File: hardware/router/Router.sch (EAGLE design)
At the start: 52 parts, among them J1 AVR_PROG, J10 RJ45-8PTH, J11 RJ45-8PTH, J12 RJ45-8PTH, J13 RJ45-8PTH, J14 RJ45-8PTH, J15 RJ45-8PTH, J16 RJ45-8PTH, J17 RASPBERRYPI_BB, J18 RJ45-8PTH, J19 RJ45-8PTH, J2 RJ45-8PTH, J3 RJ45-8PTH, J4 RJ45-8PTH, J5 RJ45-8PTH, J6 RJ45-8PTH, J7 RJ45-8PTH, J8 RJ45-8PTH, J9 RJ45-8PTH, Q1 NMOS, Q2 NMOS, Q3 NMOS, U1 ATMEGA168, U3 DS1307SO8, U6 CON-MATENLOK, Y1 32.768kHz

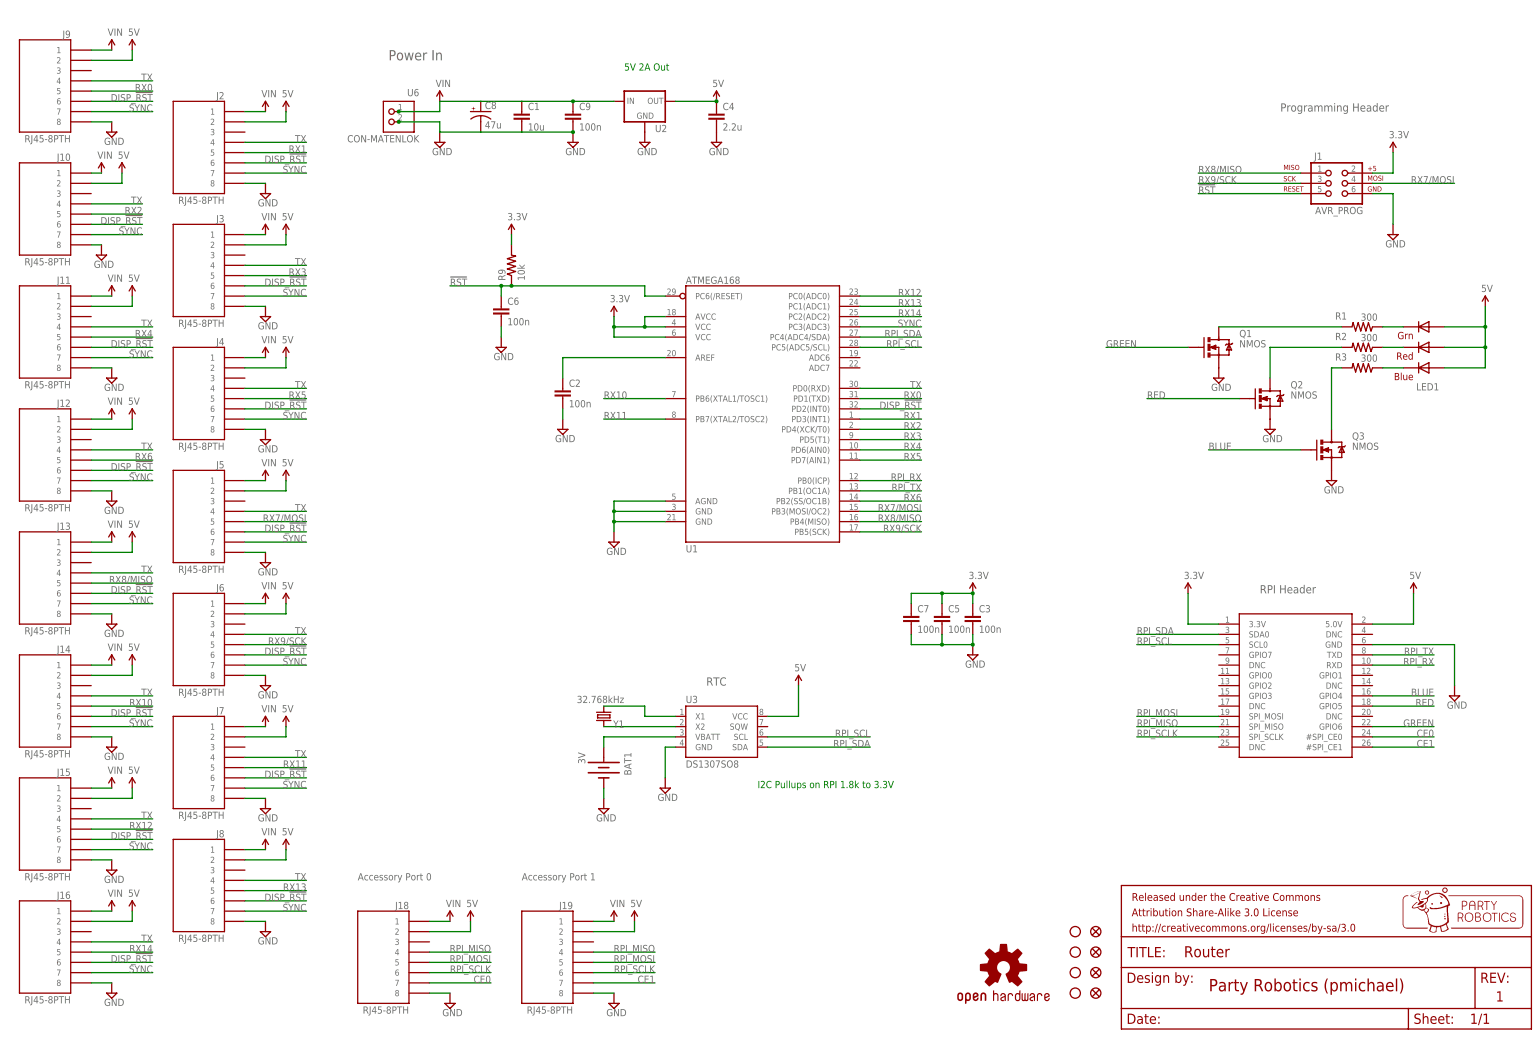
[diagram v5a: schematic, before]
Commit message: Final files that were used to CAM dispenser and router boards
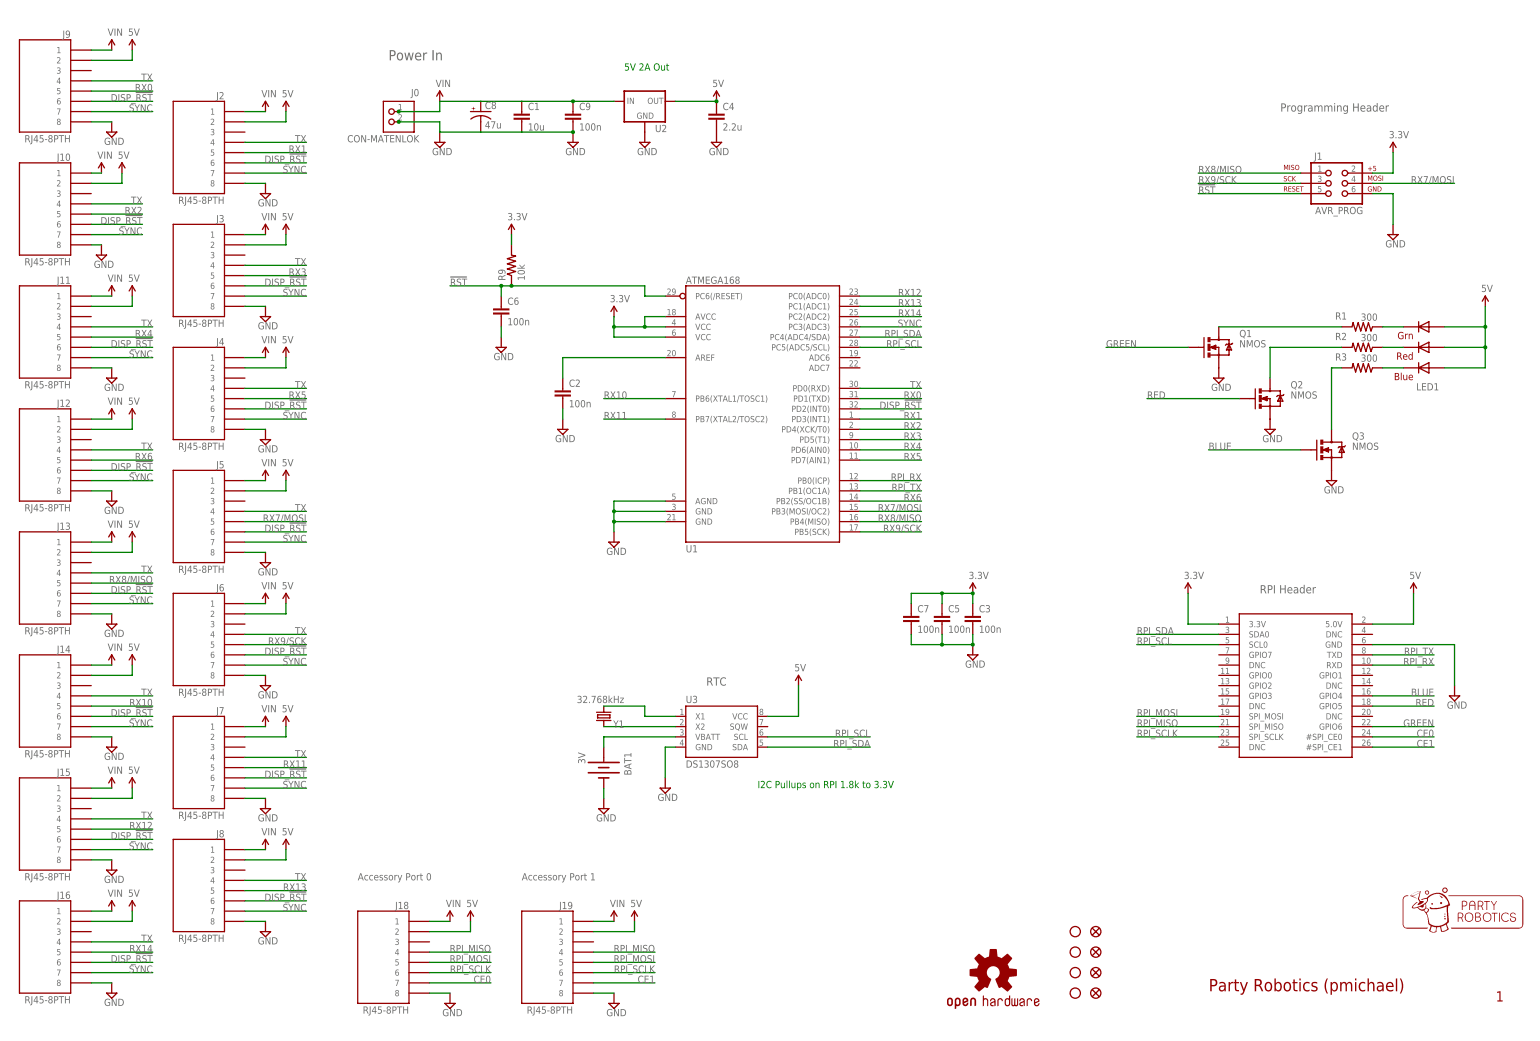
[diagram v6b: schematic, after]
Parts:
- removed FRAME3: FRAME-LETTER, SparkFun-Aesthetics:FRAME-LETTER
- removed U$5: OSHW-LOGOS, SparkFun-Aesthetics:OSHW-LOGOS
- added U$46: OSHW-LOGOM, SparkFun-Aesthetics:OSHW-LOGOM
- renumbered U6 to J0
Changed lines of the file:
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@@
 <part name="U$38" library="SparkFun-Aesthetics" deviceset="VIN" device=""/>
 <part name="SUPPLY24" library="supply2" deviceset="GND" device=""/>
-<part name="U6" library="pierre" deviceset="CON-MATENLOK" device=""/>
+<part name="J0" library="pierre" deviceset="CON-MATENLOK" device=""/>
 <part name="BAT1" library="SparkFun-Electromechanical" deviceset="BATTERY" device="12PTH" value="3V"/>
 <part name="U$18" library="SparkFun-Aesthetics" deviceset="5V" device="" value="3.3V"/>
@@
 <part name="C8" library="SparkFun-Capacitors" deviceset="CAP_POL" device="D" value="47u"/>
 <part name="C9" library="SparkFun" deviceset="CAP" device="0603-CAP" value="100n"/>
-<part name="U$5" library="SparkFun-Aesthetics" deviceset="OSHW-LOGO" device="S"/>
-<part name="FRAME3" library="SparkFun-Aesthetics" deviceset="FRAME-LETTER" device=""/>
 <part name="J17" library="pierre" deviceset="RASPBERRYPI_B" device="B"/>
+<part name="U$46" library="SparkFun-Aesthetics" deviceset="OSHW-LOGO" device="M"/>
 </parts>
 <sheets>
@@
 <instance part="U$38" gate="G$1" x="114.3" y="233.68"/>
 <instance part="SUPPLY24" gate="GND" x="114.3" y="223.52"/>
-<instance part="U6" gate="G$1" x="104.14" y="228.6" rot="MR0"/>
+<instance part="J0" gate="G$1" x="104.14" y="228.6" rot="MR0"/>
 <instance part="BAT1" gate="G$1" x="154.94" y="68.58" rot="R270"/>
 <instance part="U$18" gate="G$1" x="132.08" y="200.66"/>
@@
 <instance part="C8" gate="G$1" x="124.46" y="231.14"/>
 <instance part="C9" gate="G$1" x="147.32" y="228.6"/>
-<instance part="U$5" gate="G$1" x="254" y="19.05"/>
-<instance part="FRAME3" gate="G$2" x="283.21" y="3.81"/>
 <instance part="J17" gate="G$1" x="325.12" y="88.9"/>
+<instance part="U$46" gate="G$1" x="251.46" y="17.78"/>
 </instances>
 <busses>
@@
 <pinref part="SUPPLY24" gate="GND" pin="GND"/>
 <wire x1="114.3" y1="228.6" x2="114.3" y2="226.06" width="0.1524" layer="91"/>
-<pinref part="U6" gate="G$1" pin="2"/>
+<pinref part="J0" gate="G$1" pin="2"/>
 <junction x="104.14" y="228.6"/>
 <pinref part="C8" gate="G$1" pin="-"/>
@@
 <wire x1="114.3" y1="233.68" x2="114.3" y2="231.14" width="0.1524" layer="91"/>
 <wire x1="114.3" y1="231.14" x2="104.14" y2="231.14" width="0.1524" layer="91"/>
-<pinref part="U6" gate="G$1" pin="1"/>
+<pinref part="J0" gate="G$1" pin="1"/>
 <junction x="104.14" y="231.14"/>
 <pinref part="C8" gate="G$1" pin="+"/>

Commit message: Added Pump to RX mappings on the router schematic
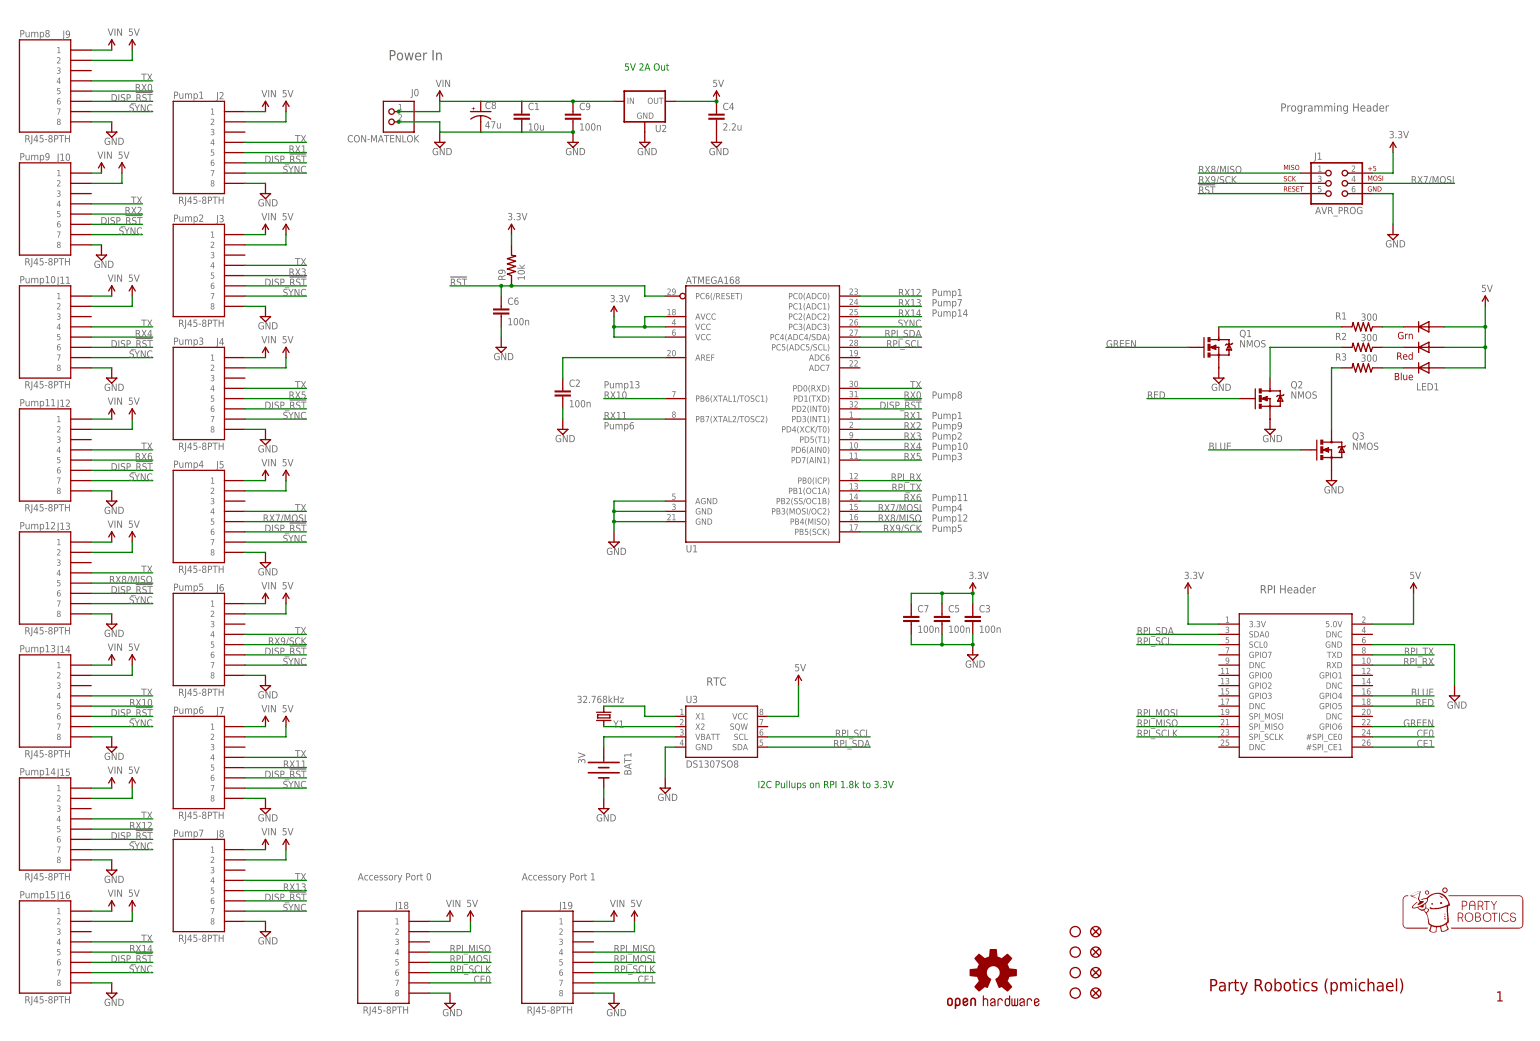
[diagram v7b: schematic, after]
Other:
- note added: "Pump1"
- note added: "Pump10"
- note added: "Pump11"
- note added: "Pump12"
- note added: "Pump13"
- note added: "Pump14"
- note added: "Pump15"
- note added: "Pump2"
- note added: "Pump3"
- note added: "Pump4"
- note added: "Pump5"
- note added: "Pump6"
- note added: "Pump7"
- note added: "Pump8"
- note added: "Pump9"
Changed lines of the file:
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@@
 <rectangle x1="363.06125" y1="38.76675" x2="363.69625" y2="38.83025" layer="94"/>
 <rectangle x1="363.25175" y1="38.83025" x2="363.50575" y2="38.89375" layer="94"/>
+<text x="48.26" y="234.315" size="1.778" layer="95">Pump1</text>
+<text x="48.26" y="203.835" size="1.778" layer="95">Pump2</text>
+<text x="10.16" y="219.075" size="1.778" layer="95">Pump9</text>
+<text x="10.16" y="249.555" size="1.778" layer="95">Pump8</text>
+<text x="10.16" y="188.595" size="1.778" layer="95">Pump10</text>
+<text x="10.16" y="158.115" size="1.778" layer="95">Pump11</text>
+<text x="48.26" y="173.355" size="1.778" layer="95">Pump3</text>
+<text x="48.26" y="142.875" size="1.778" layer="95">Pump4</text>
+<text x="10.16" y="127.635" size="1.778" layer="95">Pump12</text>
+<text x="48.26" y="112.395" size="1.778" layer="95">Pump5</text>
+<text x="10.16" y="97.155" size="1.778" layer="95">Pump13</text>
+<text x="48.26" y="81.915" size="1.778" layer="95">Pump6</text>
+<text x="10.16" y="66.675" size="1.778" layer="95">Pump14</text>
+<text x="48.26" y="51.435" size="1.778" layer="95">Pump7</text>
+<text x="10.16" y="36.195" size="1.778" layer="95">Pump15</text>
+<text x="236.22" y="185.42" size="1.778" layer="95">Pump1</text>
+<text x="236.22" y="182.88" size="1.778" layer="95">Pump7</text>
+<text x="236.22" y="180.34" size="1.778" layer="95">Pump14</text>
+<text x="236.22" y="160.02" size="1.778" layer="95">Pump8</text>
+<text x="236.22" y="154.94" size="1.778" layer="95">Pump1</text>
+<text x="236.22" y="152.4" size="1.778" layer="95">Pump9</text>
+<text x="236.22" y="149.86" size="1.778" layer="95">Pump2</text>
+<text x="236.22" y="147.32" size="1.778" layer="95">Pump10</text>
+<text x="236.22" y="144.78" size="1.778" layer="95">Pump3</text>
+<text x="236.22" y="134.62" size="1.778" layer="95">Pump11</text>
+<text x="236.22" y="132.08" size="1.778" layer="95">Pump4</text>
+<text x="236.22" y="129.54" size="1.778" layer="95">Pump12</text>
+<text x="236.22" y="127" size="1.778" layer="95">Pump5</text>
+<text x="154.94" y="162.56" size="1.778" layer="95">Pump13</text>
+<text x="154.94" y="152.4" size="1.778" layer="95">Pump6</text>
 </plain>
 <instances>
